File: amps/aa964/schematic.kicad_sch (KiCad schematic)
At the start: 69 parts, among them SW1 AC sw, SW2 gnd sw

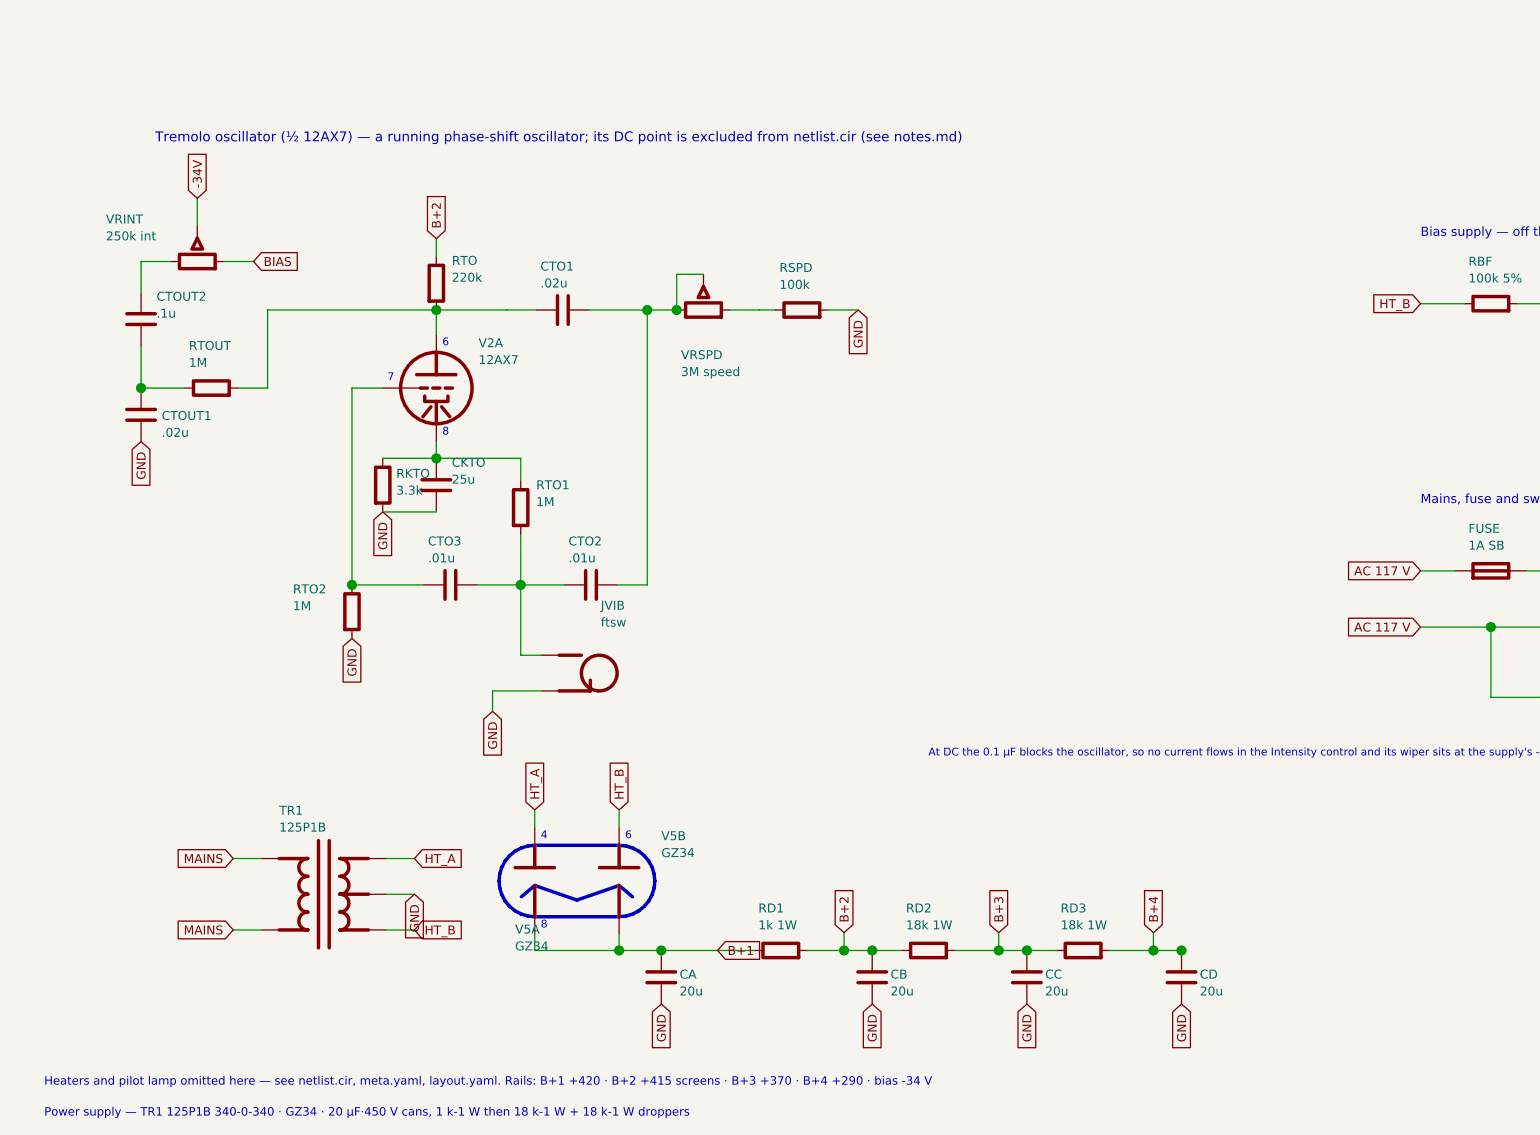
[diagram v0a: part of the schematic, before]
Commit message: Fix: schematic sheet notes no longer name repository files
Thirty-seven committed sheets rendered footnotes and section notes such as
"Heaters and PT primary omitted — see netlist.cir and meta.yaml" or
"excluded from netlist.cir (notes.md)" to visitors through KiCanvas. The
prose sweeps never counted sheets. Rewritten in the site's own words — the
netlist, the sources list, the circuit story, the parts list, the board
drawing — in 59 strings across 33 draw scripts, keeping every technical
claim as it was; the three tone sheets (6G4, 6G5, 6G6-B) are under repair
elsewhere and keep theirs for now. The sweep touched only strings passed to
the sheet's note, text, caption and footnote calls, never a path or a value.

Gates: check_schematics 40/0, connectivity 0 isolated pins;
verify_schematic_nets 40 clean; only the regenerated sheets and their served
copies changed.

Co-Authored-By: Claude Fable 5.1 <noreply@anthropic.com>
Claude-Session: https://claude.ai/code/session_01KBMfdh37HmCL2iWcBiL5J1
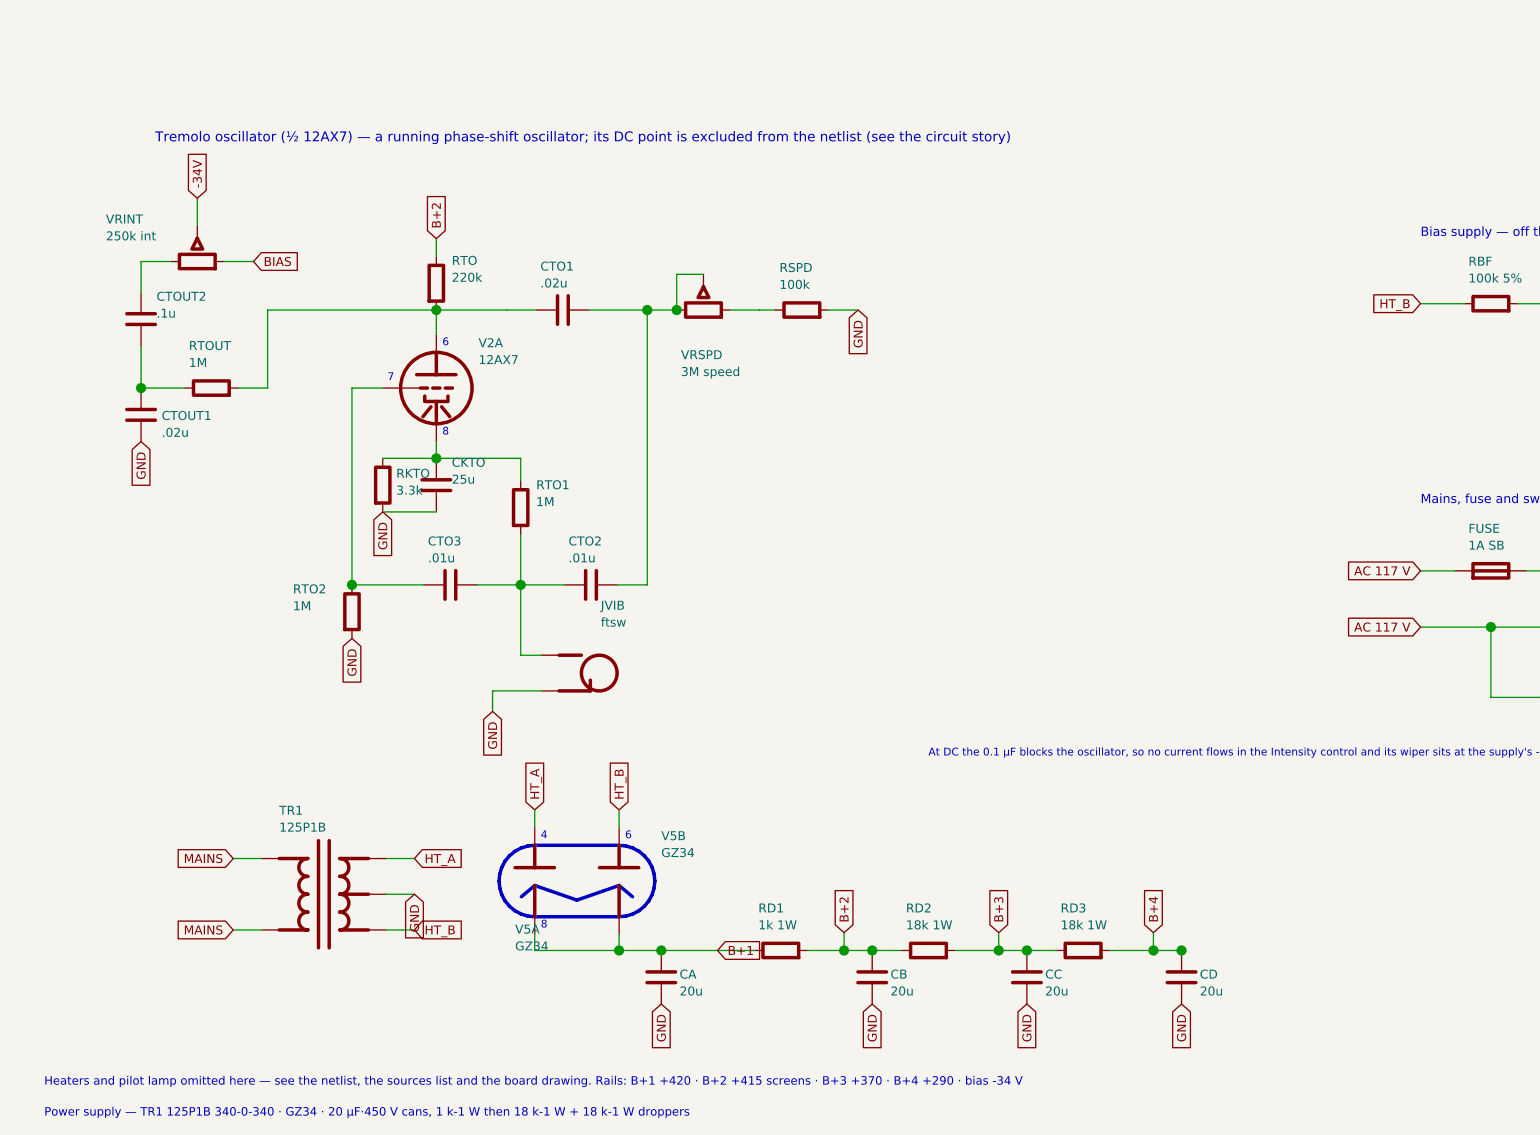
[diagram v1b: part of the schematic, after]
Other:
- note added: "Heaters and pilot lamp omitted here — see the netlist, the sources list and the board drawing. Rails: B+1 +420 · B+2 +415 screens · B+3 +370 · B+4 +290 · bias -34 V"
- note added: "Tremolo oscillator (½ 12AX7) — a running phase-shift oscillator; its DC point is excluded from the netlist (see the circuit story)"
- note removed: "Heaters and pilot lamp omitted here — see netlist.cir, meta.yaml, layout.yaml. Rails: B+1 +420 · B+2 +415 screens · B+3 +370 · B+4 +290 · bias -34 V"
- note removed: "Tremolo oscillator (½ 12AX7) — a running phase-shift oscillator; its DC point is excluded from netlist.cir (see notes.md)"
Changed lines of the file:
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@@
   (global_label "GND" (shape input) (at 322.472 66.7 270)
     (effects (font (size 1.27 1.27)) (justify right)))
-  (text "Tremolo oscillator (½ 12AX7) — a running phase-shift oscillator; its DC point is excluded from netlist.cir (see notes.md)" (at 28.4724 133.2 0)
+  (text "Tremolo oscillator (½ 12AX7) — a running phase-shift oscillator; its DC point is excluded from the netlist (see the circuit story)" (at 28.4724 133.2 0)
     (effects (font (size 1.4 1.4)) (justify left)))
   (symbol (lib_id "cx:TRIODE") (at 68.4724 168.7 0) (unit 1)
@@
   (text "6" (at 95.3224 232.47 0)
     (effects (font (size 1.1 1.1)) (justify left)))
-  (text "Heaters and pilot lamp omitted here — see netlist.cir, meta.yaml, layout.yaml. Rails: B+1 +420 · B+2 +415 screens · B+3 +370 · B+4 +290 · bias -34 V" (at 12.7 267.478 0)
+  (text "Heaters and pilot lamp omitted here — see the netlist, the sources list and the board drawing. Rails: B+1 +420 · B+2 +415 screens · B+3 +370 · B+4 +290 · bias -34 V" (at 12.7 267.478 0)
     (effects (font (size 1.2 1.2)) (justify left)))
   (text "Power supply — TR1 125P1B 340-0-340 · GZ34 · 20 µF·450 V cans, 1 k-1 W then 18 k-1 W + 18 k-1 W droppers" (at 12.7 271.878 0)

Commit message: Fix: six sheets letter valve sections and bias rows the way their factory drawings do
Sections — the board was right and the sheet printed the other half's pin
numbers (triage verdict rows, crops under the triage scratch):
  AC30 V1    JMI OS/065 (3600x2492): Brilliant grid 2 / plate 1, Normal 7 / 6
  AA964 V1   input 2/1/3, second stage 7/6/8 (6322x3926)
  AA964 V2   phase inverter 7/6/8, tremolo oscillator 2/1/3
  5F6-A V3   the 82k (input) triode on 1/2/3 on the I-EG layout (6402x3641)
  6G4 V5     the 82k triode on 1/2/3 on the A-FJ layout (2250x1269, the only copy)

Bias rows — the 5F4 (C-EG) and 5E4-A (G-EE) drawings run the series
resistor (6800 / 18K) from the transformer's bias tap INTO the selenium
rectifier. The previous commit's rows put the rectifier on the tap and the
resistor after it; both now read tap -> resistor -> rectifier -> node. The
5F4 rectifier sits clear of C17's ground flag.

Worklist after re-export: section swaps 10 -> 5 (three board re-pins in
flight, the 5E5-A whose only copy does not resolve, and the AA1164 V4 still
being read); the 5F4/5E4-A D1 rows stay MISPLACED until their boards take
the tap lead, which the board repair wave is adding.

Gates: check_schematics 40/0 (+selftest), verify_schematic_nets 40 clean,
tone gate, validate, check_value_consistency --strict 0, test_era_values,
verify_sheet_vs_board selftest 19 + drift clean after --export,
check_heaters, verify_layout_nets; regenerating every sheet changes only
these six.

Co-Authored-By: Claude Opus 5 (1M context) <noreply@anthropic.com>
Claude-Session: https://claude.ai/code/session_01KBMfdh37HmCL2iWcBiL5J1
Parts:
- V1A, V2A: Basing_unit (none) -> 2
- V1B, V2B: Basing_unit (none) -> 1
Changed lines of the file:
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@@
     (in_bom yes) (on_board yes)
     (property "Reference" "V1A" (at 66.4724 44.3 0) (effects (font (size 1.27 1.27)) (justify left)))
-    (property "Value" "7025" (at 66.4724 46.7 0) (effects (font (size 1.27 1.27)) (justify left))))
+    (property "Value" "7025" (at 66.4724 46.7 0) (effects (font (size 1.27 1.27)) (justify left)))
+    (property "Basing_unit" "2" (at 66.4724 49.1 0) (effects (font (size 1.27 1.27)) hide)))
   (wire (pts (xy 48.4724 50.7) (xy 52.8524 50.7))
     (stroke (width 0) (type default)))
@@
     (in_bom yes) (on_board yes)
     (property "Reference" "V1B" (at 154.472 44.3 0) (effects (font (size 1.27 1.27)) (justify left)))
-    (property "Value" "7025" (at 154.472 46.7 0) (effects (font (size 1.27 1.27)) (justify left))))
+    (property "Value" "7025" (at 154.472 46.7 0) (effects (font (size 1.27 1.27)) (justify left)))
+    (property "Basing_unit" "1" (at 154.472 49.1 0) (effects (font (size 1.27 1.27)) hide)))
   (wire (pts (xy 134.472 50.7) (xy 140.852 50.7))
     (stroke (width 0) (type default)))
@@
     (in_bom yes) (on_board yes)
     (property "Reference" "V2B" (at 210.472 44.3 0) (effects (font (size 1.27 1.27)) (justify left)))
-    (property "Value" "12AX7" (at 210.472 46.7 0) (effects (font (size 1.27 1.27)) (justify left))))
+    (property "Value" "12AX7" (at 210.472 46.7 0) (effects (font (size 1.27 1.27)) (justify left)))
+    (property "Basing_unit" "1" (at 210.472 49.1 0) (effects (font (size 1.27 1.27)) hide)))
   (wire (pts (xy 178.472 50.7) (xy 194.472 50.7))
     (stroke (width 0) (type default)))
@@
     (in_bom yes) (on_board yes)
     (property "Reference" "V2A" (at 74.4724 162.3 0) (effects (font (size 1.27 1.27)) (justify left)))
-    (property "Value" "12AX7" (at 74.4724 164.7 0) (effects (font (size 1.27 1.27)) (justify left))))
+    (property "Value" "12AX7" (at 74.4724 164.7 0) (effects (font (size 1.27 1.27)) (justify left)))
+    (property "Basing_unit" "2" (at 74.4724 167.1 0) (effects (font (size 1.27 1.27)) hide)))
   (wire (pts (xy 68.4724 161.08) (xy 68.4724 157.6))
     (stroke (width 0) (type default)))
@@
   (polyline (pts (xy 80.5724 241.055) (xy 82.4724 239.455) (xy 88.4724 241.535) (xy 94.4724 239.455) (xy 96.3724 241.055))
     (stroke (width 0.49) (type default) (color 197 163 255 1)) (fill (type none)))
-  (text "6" (at 61.3224 44.35 0)
-    (effects (font (size 1.1 1.1)) (justify left)))
-  (text "7" (at 53.5252 49.3 0)
-    (effects (font (size 1.1 1.1)) (justify left)))
-  (text "8" (at 61.3224 57.05 0)
-    (effects (font (size 1.1 1.1)) (justify left)))
-  (text "1" (at 149.322 44.35 0)
-    (effects (font (size 1.1 1.1)) (justify left)))
-  (text "2" (at 141.525 49.3 0)
-    (effects (font (size 1.1 1.1)) (justify left)))
-  (text "3" (at 149.322 57.05 0)
-    (effects (font (size 1.1 1.1)) (justify left)))
-  (text "1" (at 205.322 44.35 0)
-    (effects (font (size 1.1 1.1)) (justify left)))
-  (text "2" (at 197.525 49.3 0)
-    (effects (font (size 1.1 1.1)) (justify left)))
-  (text "3" (at 205.322 57.05 0)
+  (text "1" (at 61.3224 44.35 0)
+    (effects (font (size 1.1 1.1)) (justify left)))
+  (text "2" (at 53.5252 49.3 0)
+    (effects (font (size 1.1 1.1)) (justify left)))
+  (text "3" (at 61.3224 57.05 0)
+    (effects (font (size 1.1 1.1)) (justify left)))
+  (text "6" (at 149.322 44.35 0)
+    (effects (font (size 1.1 1.1)) (justify left)))
+  (text "7" (at 141.525 49.3 0)
+    (effects (font (size 1.1 1.1)) (justify left)))
+  (text "8" (at 149.322 57.05 0)
+    (effects (font (size 1.1 1.1)) (justify left)))
+  (text "6" (at 205.322 44.35 0)
+    (effects (font (size 1.1 1.1)) (justify left)))
+  (text "7" (at 197.525 49.3 0)
+    (effects (font (size 1.1 1.1)) (justify left)))
+  (text "8" (at 205.322 57.05 0)
     (effects (font (size 1.1 1.1)) (justify left)))
   (text "3" (at 267.322 21.715 0)
@@
   (text "8" (at 267.322 90.415 0)
     (effects (font (size 1.1 1.1)) (justify left)))
-  (text "6" (at 69.3224 162.35 0)
-    (effects (font (size 1.1 1.1)) (justify left)))
-  (text "7" (at 61.5252 167.3 0)
-    (effects (font (size 1.1 1.1)) (justify left)))
-  (text "8" (at 69.3224 175.05 0)
+  (text "1" (at 69.3224 162.35 0)
+    (effects (font (size 1.1 1.1)) (justify left)))
+  (text "2" (at 61.5252 167.3 0)
+    (effects (font (size 1.1 1.1)) (justify left)))
+  (text "3" (at 69.3224 175.05 0)
     (effects (font (size 1.1 1.1)) (justify left)))
   (text "4" (at 83.3224 232.47 0)

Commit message: Fix: 17 bias rectifiers and six HT diodes drawn backwards; the 6G6-B and 6G4 bias rows as their drawings show; AA1164 V4 units
Rectifier polarity has no gate. The netlists model every supply as an ideal
source, the sheet-vs-board check treats a two-terminal part as unordered, and
the boards' `cathode:` fields were copied from the sheets. Measured over all
68 diodes on 40 sheets: 18 negative-bias rectifiers had the cathode on the
negative node (a diode that way round would charge the node POSITIVE), and all
six 6G6-B HT diodes pointed away from B+. The printed negative bias on each of
those sheets falsifies the drawn orientation; the nine bias rectifiers already
right (AA1164, AA864, AB165, B15N, DR103, JTM100, M1959, M2204, 6G6-B) show
the idiom. Flipped: 5E4-A, 5E5-A, 5E6-A, 5F10, 5F4, 5F6, 5F6-A, 5F8-A, 5G9,
6G2, 6G3, 6G4, 6G5, AA964, AB763, AB763 Super, AB763 Twin, JTM45 (the
M1987's is with the Marshall board repair) and the 6G6-B's DR1-DR6. The
5F8-A board, which had copied its sheet, has the band moved to the tap side;
the other boards' bands are with the board-repair wave. A gate is next.

6G6-B bias. E-FB (6431x3364): the 1K 1W rises from TR1's SECOND secondary
terminal, a bias tap between the upper HT end and the grounded centre tap,
to the diode's + end. The sheet fed the diode from the HT end with the 1K
after it. T1 now carries its tap pin and the row reads tap -> 1K -> diode ->
-54 V. (The triage had read "HT end"; the native crop shows the tap.)

6G4 bias. A-FJ, read natively: tap -> rectifier -> 8 uF -> 10K -> the -55 V
node, which carries a second 8 uF and the 56K to ground as a bleeder. The
sheet fed the rectifier from an HT end, drew the 56K in series and carried
one capacitor. CBIAS2 joins the parts list, and RBIAS1's role now says
bleeder.

AA1164 V4. The K-FD sheet prints the phase inverter 7/6/8 and the tremolo
oscillator 2/1/3 (5554x4346); the sheet had them the other way round.

Gates: check_schematics 40/0 (+selftest), verify_schematic_nets 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
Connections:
- net BIAS: now also DBIAS.1 (A); no longer DBIAS.2 (K)
- net at RBF.2: now also DBIAS.2 (K); no longer DBIAS.1 (A)
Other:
- moved on the sheet: DBIAS
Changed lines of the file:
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@@
   (wire (pts (xy 222.282 156.7) (xy 226.472 156.7))
     (stroke (width 0) (type default)))
-  (symbol (lib_id "cx:DIODE_SS") (at 231.552 156.7 0) (unit 1)
+  (symbol (lib_id "cx:DIODE_SS") (at 231.552 156.7 180) (unit 1)
     (in_bom yes) (on_board yes)
     (property "Reference" "DBIAS" (at 229.552 151.3 0) (effects (font (size 1.27 1.27)) (justify left)))

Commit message: Fix: the 6G5's rectifier was connected to nothing; 17 sheets shorted the mains by naming both leads alike
6G5 power supply. The sheet drew four diodes as a "silicon bridge" whose
HT_A/HT_B labels stopped 6 mm short of their wires. D1/D2's anodes sat on
the tremolo's cathode node (a tremolo wire's end touched the old diode
stub), D3/D4 ran from ground to the reservoir, and TR1's centre tap floated
under an open-pin waiver whose stated reason was the bridge itself.
A-FJ (Schematic Heaven 2153x1437, read enlarged): each HT end of TR1 runs
through a leg of three silicon diodes, every + (cathode) toward the +460 V
reservoir; the centre tap is grounded; TR1's second secondary terminal is a
bias tap feeding the 6G4's network part for part: rectifier, 8-150, 10K,
then 8-150 and a 56K bleeder at the -55 V line. Redrawn as the drawing
shows: D1-D6, TR1 with its tap pin, the centre tap to ground, the bias
network (CBIAS 25 uF -> 8 uF; RBIAS2, CBIAS2, RBIAS1 added), the waiver
deleted, and the notes, meta, netlist header and parts list no longer say
bridge. Not yet carried: the drawing's second 20-600 at the reservoir and
the standby switch (this sheet omits chassis switches by its own note);
and the tremolo ladder still runs through the transformer's corner of the
sheet, a layout clash rather than a connection, queued for its own redraw.

Mains. Two global labels with one name are one net. 16 of 24 power
transformers on the sheets carried a label named MAINS on both primary
leads, so the winding's two pins were one net: 5E4-A, 5E5-A, 5F4, 5G9,
6161, 6G2, 6G3, 6G4, AA1164, AA764, AA764-Vibro, AA964, AB763, AB763
Super, AB763 Twin, GA-40. The 6G5's loop ran from one MAINS label through
switch, fuse and winding back to the same name. No gate models the primary,
so a copy-pasted idiom did this. The second lead is now MAINS N, the AC15's
idiom; the AA1164's and AA964's second AC row, drawn under the first row's
name, is the neutral. The death and across-the-line caps stay on the le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
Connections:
- net AC 117 V: no longer SW1.2, SW2.1, TR1.1 (PRI_1), TR1.2 (PRI_2)
- new net AC N: SW2.1, TR1.2 (PRI_2)
- new net MAINS: SW1.2, TR1.1 (PRI_1)
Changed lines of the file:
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@@
   (wire (pts (xy 43.5824 245.78) (xy 39.5824 245.78))
     (stroke (width 0) (type default)))
-  (global_label "MAINS" (shape input) (at 39.5824 245.78 180)
+  (global_label "MAINS N" (shape input) (at 39.5824 245.78 180)
     (effects (font (size 1.27 1.27)) (justify right)))
   (wire (pts (xy 61.3624 235.62) (xy 65.3624 235.62))
@@
   (global_label "MAINS" (shape input) (at 248.472 194.7 0)
     (effects (font (size 1.27 1.27)) (justify left)))
-  (global_label "AC 117 V" (shape input) (at 208.472 202.7 180)
+  (global_label "AC N" (shape input) (at 208.472 202.7 180)
     (effects (font (size 1.27 1.27)) (justify right)))
   (wire (pts (xy 208.472 202.7) (xy 218.472 202.7))
@@
   (wire (pts (xy 218.472 202.7) (xy 248.472 202.7))
     (stroke (width 0) (type default)))
-  (global_label "MAINS" (shape input) (at 248.472 202.7 0)
+  (global_label "MAINS N" (shape input) (at 248.472 202.7 0)
     (effects (font (size 1.27 1.27)) (justify left)))
   (junction (at 218.472 202.7) (diameter 1.448) (color 0 0 0 0))
